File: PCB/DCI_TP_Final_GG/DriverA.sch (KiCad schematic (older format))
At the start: 18 parts

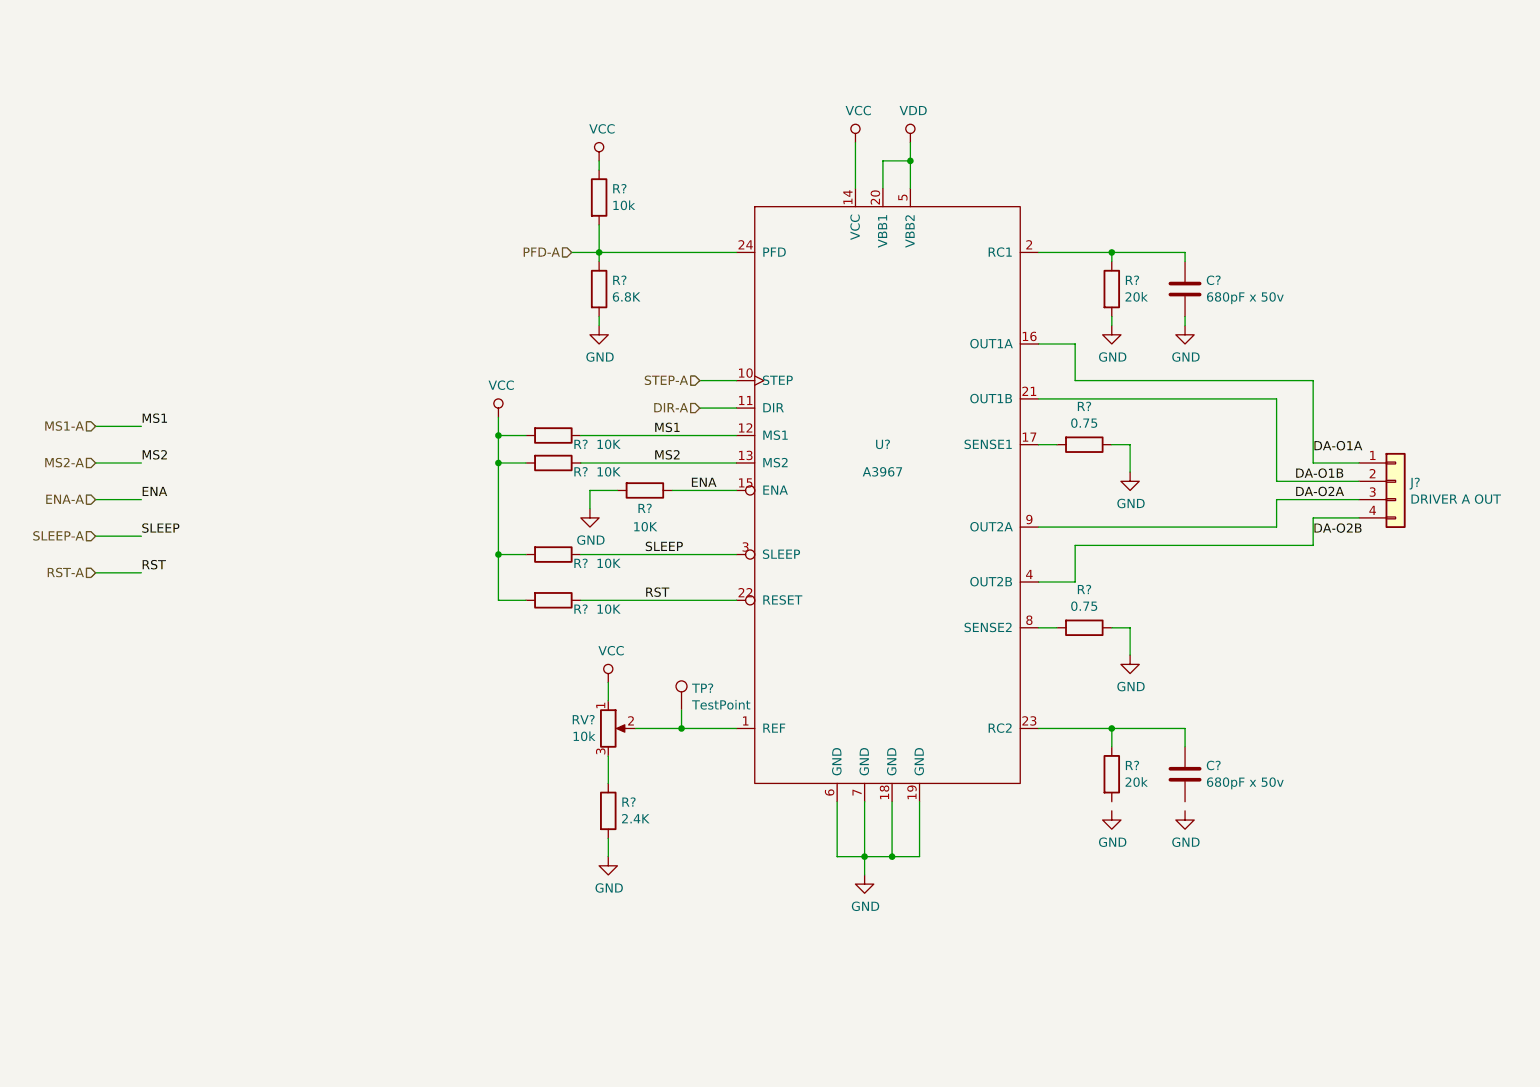
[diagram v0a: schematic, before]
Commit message: Hoja de fuente y conectores completa.
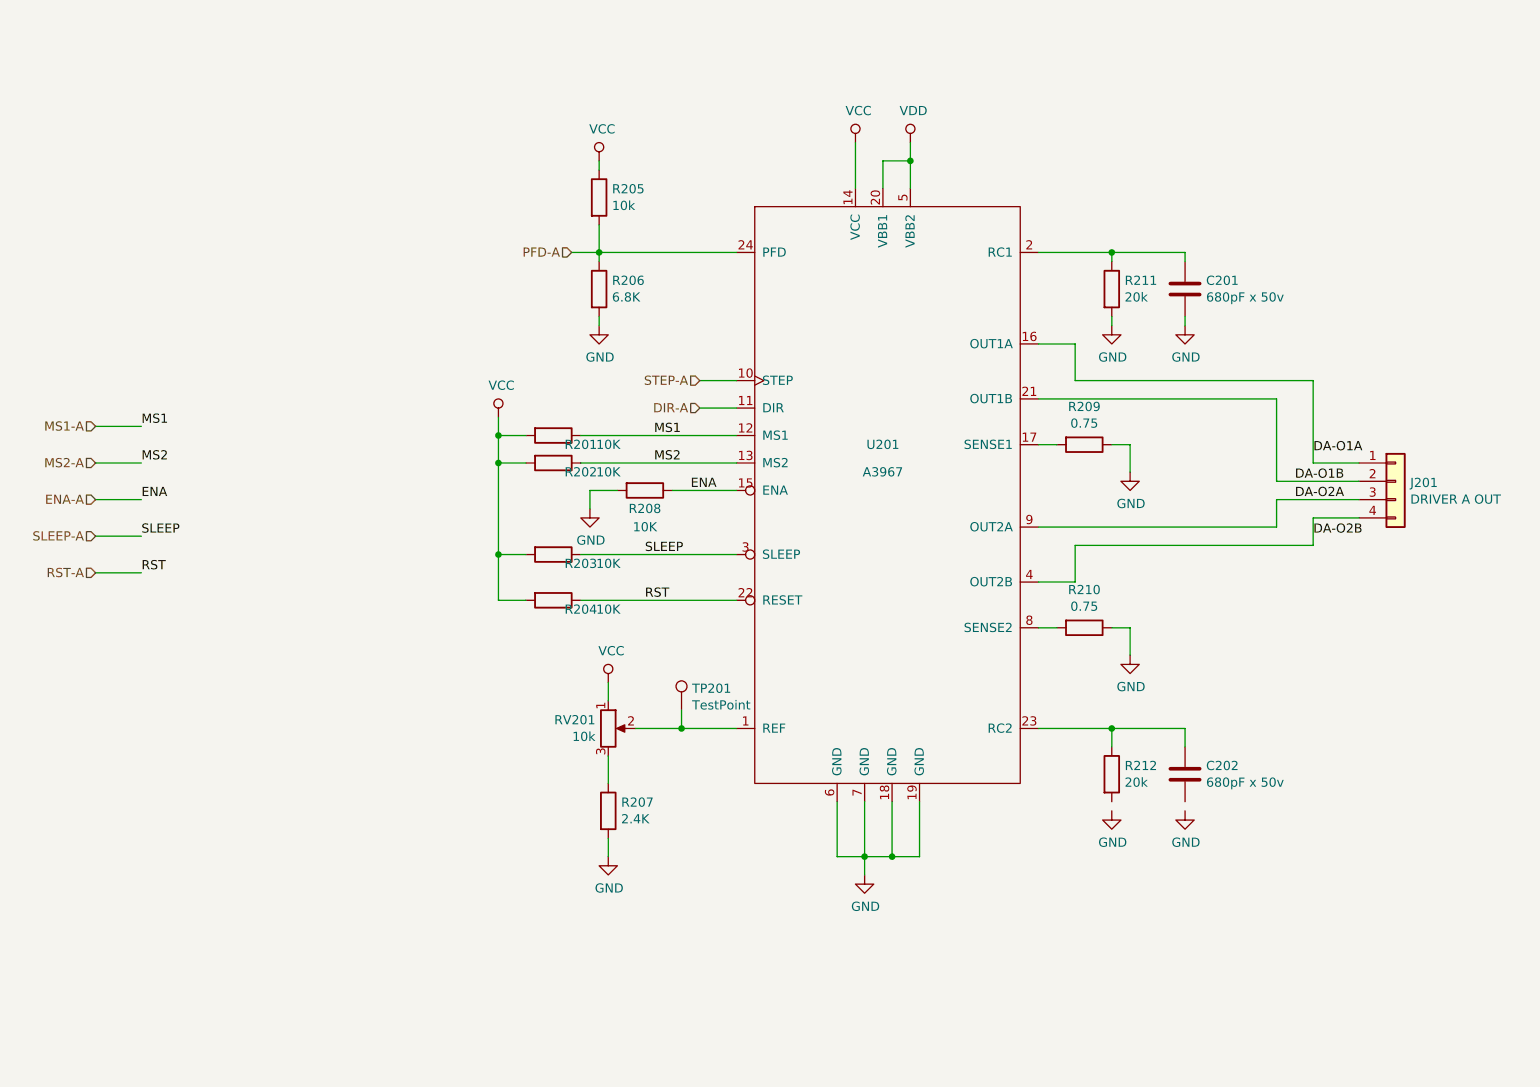
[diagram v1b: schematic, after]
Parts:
- TP201: renamed from TP?; footprint (none) -> TestPoint:TestPoint_Pad_D2.0mm
- gave numbers to parts that had none: 17
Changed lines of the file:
@@
 encoding utf-8
 Sheet 2 4
-Title ""
-Date ""
+Title "Replica Dual EasyDriver v4.5"
+Date "2019-10-02"
 Rev ""
-Comp ""
+Comp "Gonzalo Gontad - CESE-FIUBA"
 Comment1 ""
 Comment2 ""
@@
 $EndDescr
 $Comp
-L DCI_GG_CESE_FIUBA:A3967 U?
+L DCI_GG_CESE_FIUBA:A3967 U201
 U 1 1 5D973B9E
 P 3250 1150
-F 0 "U?" H 5800 -1100 50  0000 C CNN
+F 0 "U201" H 5800 -1100 50  0000 C CNN
 F 1 "A3967" H 5800 -1250 50  0000 C CNN
 F 2 "Package_SO:SOIC-24W_7.5x15.4mm_P1.27mm" V 6100 -1300 50  0001 C CNN
@@
 Connection ~ 5850 5650
 $Comp
-L power:GND #PWR?
+L power:GND #PWR0208
 U 1 1 5D96B0D6
 P 5700 5750
-F 0 "#PWR?" H 5700 5500 50  0001 C CNN
+F 0 "#PWR0208" H 5700 5500 50  0001 C CNN
 F 1 "GND" H 5705 5577 50  0000 C CNN
 F 2 "" H 5700 5750 50  0001 C CNN
@@
 	5700 5750 5700 5650
 $Comp
-L power:VCC #PWR?
+L power:VCC #PWR0207
 U 1 1 5D96D6E9
 P 5650 1750
-F 0 "#PWR?" H 5650 1600 50  0001 C CNN
+F 0 "#PWR0207" H 5650 1600 50  0001 C CNN
 F 1 "VCC" H 5667 1923 50  0000 C CNN
 F 2 "" H 5650 1750 50  0001 C CNN
@@
 $EndComp
 $Comp
-L power:VDD #PWR?
+L power:VDD #PWR0209
 U 1 1 5D96DCE4
 P 5950 1750
-F 0 "#PWR?" H 5950 1600 50  0001 C CNN
+F 0 "#PWR0209" H 5950 1600 50  0001 C CNN
 F 1 "VDD" H 5967 1923 50  0000 C CNN
 F 2 "" H 5950 1750 50  0001 C CNN
@@
 	5950 1850 5950 1750
 $Comp
-L Connector_Generic:Conn_01x04 J?
+L Connector_Generic:Conn_01x04 J201
 U 1 1 5D96F0CD
 P 8600 3600
-F 0 "J?" H 8680 3592 50  0000 L CNN
+F 0 "J201" H 8680 3592 50  0000 L CNN
 F 1 "DRIVER A OUT" H 8680 3501 50  0000 L CNN
 F 2 "TerminalBlock:TerminalBlock_Altech_AK300-4_P5.00mm" H 8600 3600 50  0001 C CNN
@@
 	6650 3850 7950 3850
 $Comp
-L Device:R R?
+L Device:R R209
 U 1 1 5D9772A0
 P 6900 3400
-F 0 "R?" V 6693 3400 50  0000 C CNN
+F 0 "R209" V 6693 3400 50  0000 C CNN
 F 1 "0.75" V 6784 3400 50  0000 C CNN
 F 2 "Resistor_SMD:R_0805_2012Metric" V 6830 3400 50  0001 C CNN
@@
 $EndComp
 $Comp
-L Device:R R?
+L Device:R R210
 U 1 1 5D977AE8
 P 6900 4400
-F 0 "R?" V 6693 4400 50  0000 C CNN
+F 0 "R210" V 6693 4400 50  0000 C CNN
 F 1 "0.75" V 6784 4400 50  0000 C CNN
 F 2 "Resistor_SMD:R_0805_2012Metric" V 6830 4400 50  0001 C CNN
@@
 $EndComp
 $Comp
-L power:GND #PWR?
+L power:GND #PWR0213
 U 1 1 5D978265
 P 7150 4550
-F 0 "#PWR?" H 7150 4300 50  0001 C CNN
+F 0 "#PWR0213" H 7150 4300 50  0001 C CNN
 F 1 "GND" H 7155 4377 50  0000 C CNN
 F 2 "" H 7150 4550 50  0001 C CNN
@@
 $EndComp
 $Comp
-L power:GND #PWR?
+L power:GND #PWR0212
 U 1 1 5D978D58
 P 7150 3550
-F 0 "#PWR?" H 7150 3300 50  0001 C CNN
+F 0 "#PWR0212" H 7150 3300 50  0001 C CNN
 F 1 "GND" H 7155 3377 50  0000 C CNN
 F 2 "" H 7150 3550 50  0001 C CNN
@@
 	7150 4400 7150 4550
 $Comp
-L Device:R R?
+L Device:R R212
 U 1 1 5D97A873
 P 7050 5200
-F 0 "R?" H 7120 5246 50  0000 L CNN
+F 0 "R212" H 7120 5246 50  0000 L CNN
 F 1 "20k" H 7120 5155 50  0000 L CNN
 F 2 "Resistor_SMD:R_0805_2012Metric" V 6980 5200 50  0001 C CNN
@@
 $EndComp
 $Comp
-L Device:C C?
+L Device:C C202
 U 1 1 5D97AE7B
 P 7450 5200
-F 0 "C?" H 7565 5246 50  0000 L CNN
+F 0 "C202" H 7565 5246 50  0000 L CNN
 F 1 "680pF x 50v" H 7565 5155 50  0000 L CNN
 F 2 "Capacitor_SMD:C_0805_2012Metric" H 7488 5050 50  0001 C CNN
@@
 $EndComp
 $Comp
-L Device:R R?
+L Device:R R211
 U 1 1 5D97D707
 P 7050 2550
-F 0 "R?" H 7120 2596 50  0000 L CNN
+F 0 "R211" H 7120 2596 50  0000 L CNN
 F 1 "20k" H 7120 2505 50  0000 L CNN
 F 2 "Resistor_SMD:R_0805_2012Metric" V 6980 2550 50  0001 C CNN
@@
 $EndComp
 $Comp
-L Device:C C?
+L Device:C C201
 U 1 1 5D97D712
 P 7450 2550
-F 0 "C?" H 7565 2596 50  0000 L CNN
+F 0 "C201" H 7565 2596 50  0000 L CNN
 F 1 "680pF x 50v" H 7565 2505 50  0000 L CNN
 F 2 "Capacitor_SMD:C_0805_2012Metric" H 7488 2400 50  0001 C CNN
@@
 $EndComp
 $Comp
-L power:GND #PWR?
+L power:GND #PWR0210
 U 1 1 5D9821C6
 P 7050 2750
-F 0 "#PWR?" H 7050 2500 50  0001 C CNN
+F 0 "#PWR0210" H 7050 2500 50  0001 C CNN
 F 1 "GND" H 7055 2577 50  0000 C CNN
 F 2 "" H 7050 2750 50  0001 C CNN
@@
 $EndComp
 $Comp
-L power:GND #PWR?
+L power:GND #PWR0214
 U 1 1 5D982982
 P 7450 2750
-F 0 "#PWR?" H 7450 2500 50  0001 C CNN
+F 0 "#PWR0214" H 7450 2500 50  0001 C CNN
 F 1 "GND" H 7455 2577 50  0000 C CNN
 F 2 "" H 7450 2750 50  0001 C CNN
@@
 $EndComp
 $Comp
-L power:GND #PWR?
+L power:GND #PWR0211
 U 1 1 5D982F91
 P 7050 5400
-F 0 "#PWR?" H 7050 5150 50  0001 C CNN
+F 0 "#PWR0211" H 7050 5150 50  0001 C CNN
 F 1 "GND" H 7055 5227 50  0000 C CNN
 F 2 "" H 7050 5400 50  0001 C CNN
@@
 $EndComp
 $Comp
-L power:GND #PWR?
+L power:GND #PWR0215
 U 1 1 5D983199
 P 7450 5400
-F 0 "#PWR?" H 7450 5150 50  0001 C CNN
+F 0 "#PWR0215" H 7450 5150 50  0001 C CNN
 F 1 "GND" H 7455 5227 50  0000 C CNN
 F 2 "" H 7450 5400 50  0001 C CNN
@@
 	7050 4950 6650 4950
 $Comp
-L Device:R R?
+L Device:R R206
 U 1 1 5D9954A4
 P 4250 2550
-F 0 "R?" H 4320 2596 50  0000 L CNN
+F 0 "R206" H 4320 2596 50  0000 L CNN
 F 1 "6.8K" H 4320 2505 50  0000 L CNN
 F 2 "Resistor_SMD:R_0805_2012Metric" V 4180 2550 50  0001 C CNN
@@
 $EndComp
 $Comp
-L Device:R R?
+L Device:R R205
 U 1 1 5D997CC8
 P 4250 2050
-F 0 "R?" H 4320 2096 50  0000 L CNN
+F 0 "R205" H 4320 2096 50  0000 L CNN
 F 1 "10k" H 4320 2005 50  0000 L CNN
 F 2 "Resistor_SMD:R_0805_2012Metric" V 4180 2050 50  0001 C CNN
@@
 $EndComp
 $Comp
-L power:GND #PWR?
+L power:GND #PWR0204
 U 1 1 5D9982F2
 P 4250 2750
-F 0 "#PWR?" H 4250 2500 50  0001 C CNN
+F 0 "#PWR0204" H 4250 2500 50  0001 C CNN
 F 1 "GND" H 4255 2577 50  0000 C CNN
 F 2 "" H 4250 2750 50  0001 C CNN
@@
 $EndComp
 $Comp
-L power:VCC #PWR?
+L power:VCC #PWR0203
 U 1 1 5D998ACC
 P 4250 1850
-F 0 "#PWR?" H 4250 1700 50  0001 C CNN
+F 0 "#PWR0203" H 4250 1700 50  0001 C CNN
 F 1 "VCC" H 4267 2023 50  0000 C CNN
 F 2 "" H 4250 1850 50  0001 C CNN
@@
 	4250 1850 4250 1900
 $Comp
-L Device:R_POT RV?
+L Device:R_POT RV201
 U 1 1 5D9A1651
 P 4300 4950
-F 0 "RV?" H 4230 4996 50  0000 R CNN
+F 0 "RV201" H 4230 4996 50  0000 R CNN
 F 1 "10k" H 4230 4905 50  0000 R CNN
 F 2 "Potentiometer_SMD:Potentiometer_Vishay_TS53YJ_Vertical" H 4300 4950 50  0001 C CNN
@@
 $EndComp
 $Comp
-L Device:R R?
+L Device:R R207
 U 1 1 5D9A2466
 P 4300 5400
-F 0 "R?" H 4370 5446 50  0000 L CNN
+F 0 "R207" H 4370 5446 50  0000 L CNN
 F 1 "2.4K" H 4370 5355 50  0000 L CNN
 F 2 "Resistor_SMD:R_0805_2012Metric" V 4230 5400 50  0001 C CNN
@@
 $EndComp
 $Comp
-L power:GND #PWR?
+L power:GND #PWR0206
 U 1 1 5D9A2951
 P 4300 5650
-F 0 "#PWR?" H 4300 5400 50  0001 C CNN
+F 0 "#PWR0206" H 4300 5400 50  0001 C CNN
 F 1 "GND" H 4305 5477 50  0000 C CNN
 F 2 "" H 4300 5650 50  0001 C CNN
@@
 $EndComp
 $Comp
-L power:VCC #PWR?
+L power:VCC #PWR0205
 U 1 1 5D9A2DAA
 P 4300 4700
-F 0 "#PWR?" H 4300 4550 50  0001 C CNN
+F 0 "#PWR0205" H 4300 4550 50  0001 C CNN
 F 1 "VCC" H 4317 4873 50  0000 C CNN
 F 2 "" H 4300 4700 50  0001 C CNN
@@
 $EndComp
 $Comp
-L Connector:TestPoint TP?
+L Connector:TestPoint TP201
 U 1 1 5D9A33E4
 P 4700 4850
-F 0 "TP?" H 4758 4968 50  0000 L CNN
+F 0 "TP201" H 4758 4968 50  0000 L CNN
 F 1 "TestPoint" H 4758 4877 50  0000 L CNN
-F 2 "" H 4900 4850 50  0001 C CNN
+F 2 "TestPoint:TestPoint_Pad_D2.0mm" H 4900 4850 50  0001 C CNN
 F 3 "~" H 4900 4850 50  0001 C CNN
 	1    4700 4850
@@
 	4700 4950 4450 4950
 $Comp
-L Device:R R?
+L Device:R R208
 U 1 1 5D9AD238
 P 4500 3650
-F 0 "R?" V 4600 3650 50  0000 C CNN
+F 0 "R208" V 4600 3650 50  0000 C CNN
 F 1 "10K" V 4700 3650 50  0000 C CNN
 F 2 "Resistor_SMD:R_0805_2012Metric" V 4430 3650 50  0001 C CNN
@@
 $EndComp
 $Comp
-L power:GND #PWR?
+L power:GND #PWR0202
 U 1 1 5D9ADB97
 P 4200 3750
-F 0 "#PWR?" H 4200 3500 50  0001 C CNN
+F 0 "#PWR0202" H 4200 3500 50  0001 C CNN
 F 1 "GND" H 4205 3577 50  0000 C CNN
 F 2 "" H 4200 3750 50  0001 C CNN
@@
 	4200 3650 4200 3750
 $Comp
-L Device:R R?
+L Device:R R202
 U 1 1 5D9B1238
 P 4000 3500
-F 0 "R?" V 4050 3650 50  0000 C CNN
+F 0 "R202" V 4050 3650 50  0000 C CNN
 F 1 "10K" V 4050 3800 50  0000 C CNN
 F 2 "Resistor_SMD:R_0805_2012Metric" V 3930 3500 50  0001 C CNN
@@
 $EndComp
 $Comp
-L Device:R R?
+L Device:R R201
 U 1 1 5D9B192B
 P 4000 3350
-F 0 "R?" V 4050 3500 50  0000 C CNN
+F 0 "R201" V 4050 3500 50  0000 C CNN
 F 1 "10K" V 4050 3650 50  0000 C CNN
 F 2 "Resistor_SMD:R_0805_2012Metric" V 3930 3350 50  0001 C CNN
@@
 	4150 3500 5000 3500
 $Comp
-L Device:R R?
+L Device:R R203
 U 1 1 5D9B8041
 P 4000 4000
-F 0 "R?" V 4050 4150 50  0000 C CNN
+F 0 "R203" V 4050 4150 50  0000 C CNN
 F 1 "10K" V 4050 4300 50  0000 C CNN
 F 2 "Resistor_SMD:R_0805_2012Metric" V 3930 4000 50  0001 C CNN
@@
 $EndComp
 $Comp
-L Device:R R?
+L Device:R R204
 U 1 1 5D9B8586
 P 4000 4250
-F 0 "R?" V 4050 4400 50  0000 C CNN
+F 0 "R204" V 4050 4400 50  0000 C CNN
 F 1 "10K" V 4050 4550 50  0000 C CNN
 F 2 "Resistor_SMD:R_0805_2012Metric" V 3930 4250 50  0001 C CNN
@@
 	3700 3500 3700 4000
 $Comp
-L power:VCC #PWR?
+L power:VCC #PWR0201
 U 1 1 5D9C167C
 P 3700 3250
-F 0 "#PWR?" H 3700 3100 50  0001 C CNN
+F 0 "#PWR0201" H 3700 3100 50  0001 C CNN
 F 1 "VCC" H 3717 3423 50  0000 C CNN
 F 2 "" H 3700 3250 50  0001 C CNN

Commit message: Se completo el esquematico y documentación. El esquematico esta listo para una primera revisión.
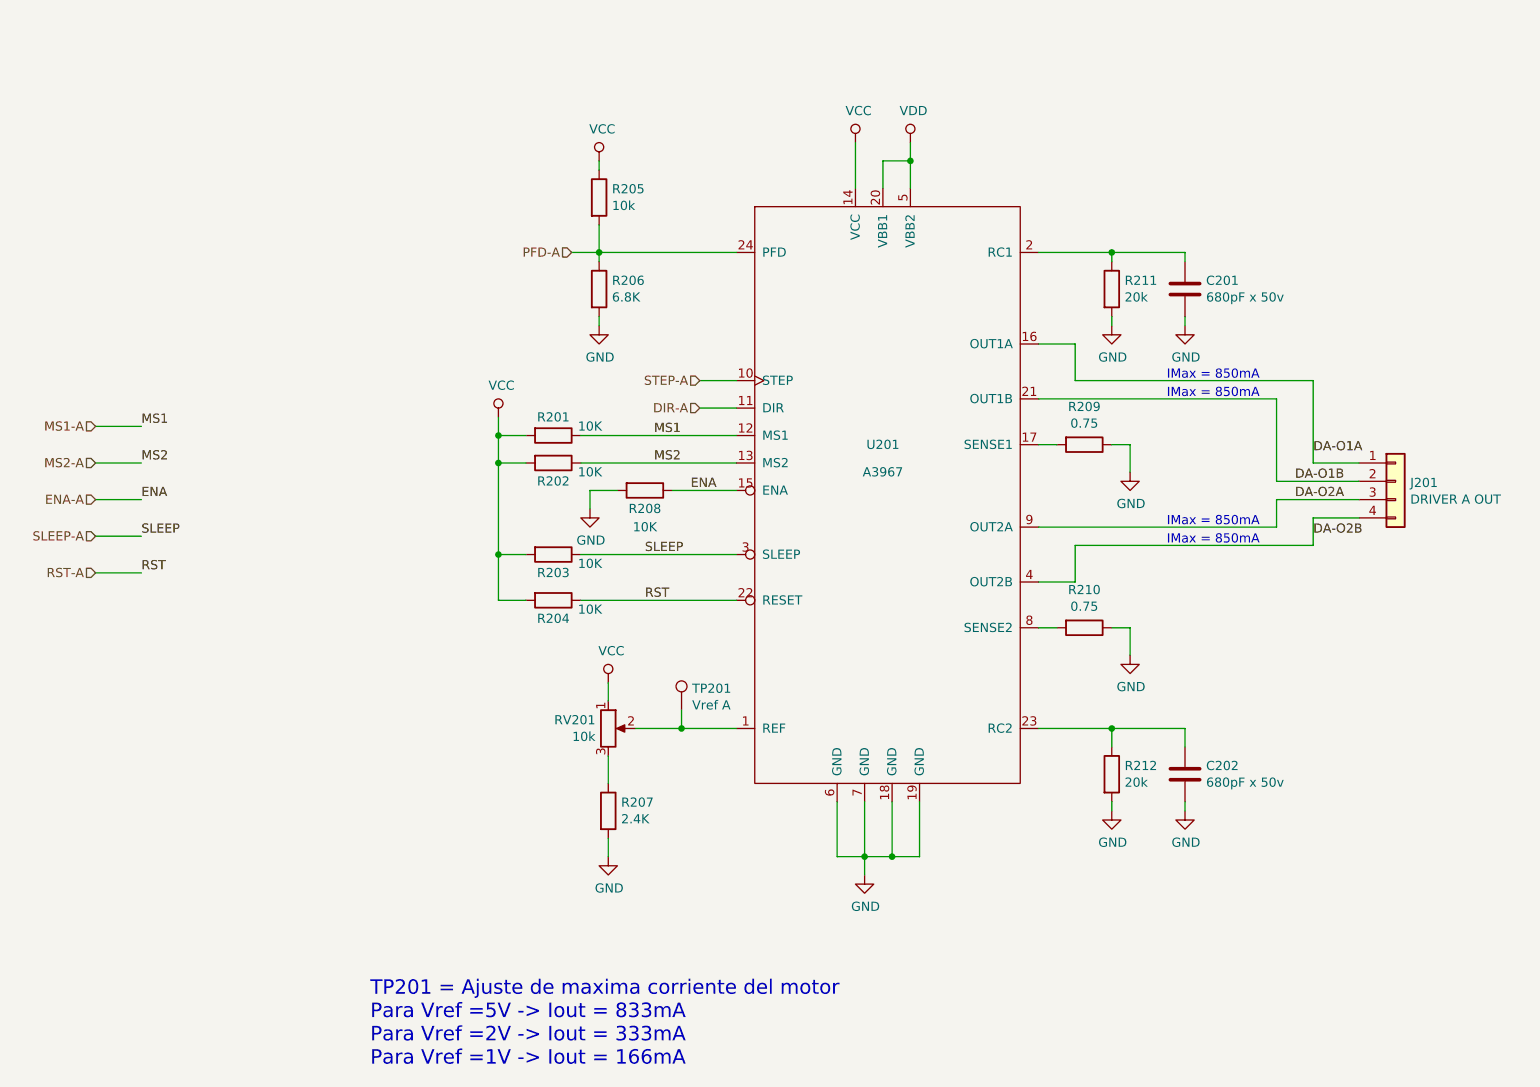
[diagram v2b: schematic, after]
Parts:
- TP201: value TestPoint -> Vref A
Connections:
- net GND: now also C202.2, R212.2
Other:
- note added: "IMax = 850mA"
- note added: "TP201 = Ajuste de maxima corriente del motor\nPara Vref =5V -> Iout = 833mA\nPara Vref =2V -> Iout = 333mA\nPara Vref =1V -> Iout = 166mA"
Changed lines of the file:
@@
 P 4700 4850
 F 0 "TP201" H 4758 4968 50  0000 L CNN
-F 1 "TestPoint" H 4758 4877 50  0000 L CNN
+F 1 "Vref A" H 4758 4877 50  0000 L CNN
 F 2 "TestPoint:TestPoint_Pad_D2.0mm" H 4900 4850 50  0001 C CNN
 F 3 "~" H 4900 4850 50  0001 C CNN
@@
 U 1 1 5D9B1238
 P 4000 3500
-F 0 "R202" V 4050 3650 50  0000 C CNN
-F 1 "10K" V 4050 3800 50  0000 C CNN
+F 0 "R202" V 4100 3500 50  0000 C CNN
+F 1 "10K" V 4050 3700 50  0000 C CNN
 F 2 "Resistor_SMD:R_0805_2012Metric" V 3930 3500 50  0001 C CNN
 F 3 "" H 4000 3500 50  0001 C CNN
@@
 U 1 1 5D9B192B
 P 4000 3350
-F 0 "R201" V 4050 3500 50  0000 C CNN
-F 1 "10K" V 4050 3650 50  0000 C CNN
+F 0 "R201" V 3900 3350 50  0000 C CNN
+F 1 "10K" V 3950 3550 50  0000 C CNN
 F 2 "Resistor_SMD:R_0805_2012Metric" V 3930 3350 50  0001 C CNN
 F 3 "" H 4000 3350 50  0001 C CNN
@@
 U 1 1 5D9B8041
 P 4000 4000
-F 0 "R203" V 4050 4150 50  0000 C CNN
-F 1 "10K" V 4050 4300 50  0000 C CNN
+F 0 "R203" V 4100 4000 50  0000 C CNN
+F 1 "10K" V 4050 4200 50  0000 C CNN
 F 2 "Resistor_SMD:R_0805_2012Metric" V 3930 4000 50  0001 C CNN
 F 3 "" H 4000 4000 50  0001 C CNN
@@
 U 1 1 5D9B8586
 P 4000 4250
-F 0 "R204" V 4050 4400 50  0000 C CNN
-F 1 "10K" V 4050 4550 50  0000 C CNN
+F 0 "R204" V 4100 4250 50  0000 C CNN
+F 1 "10K" V 4050 4450 50  0000 C CNN
 F 2 "Resistor_SMD:R_0805_2012Metric" V 3930 4250 50  0001 C CNN
 F 3 "" H 4000 4250 50  0001 C CNN
@@
 Text Label 8150 3900 0    50   ~ 0
 DA-O2B
+Wire Wire Line
+	7450 5350 7450 5400
+Wire Wire Line
+	7050 5350 7050 5400
+Text Notes 7350 3050 0    50   ~ 0
+IMax = 850mA
+Text Notes 7350 3150 0    50   ~ 0
+IMax = 850mA
+Text Notes 7350 3850 0    50   ~ 0
+IMax = 850mA
+Text Notes 7350 3950 0    50   ~ 0
+IMax = 850mA
+Text Notes 3000 6800 0    79   ~ 0
+TP201 = Ajuste de maxima corriente del motor\nPara Vref =5V -> Iout = 833mA\nPara Vref =2V -> Iout = 333mA\nPara Vref =1V -> Iout = 166mA
 $EndSCHEMATC

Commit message: Inicio etapa de desarrollo de PCB, agrego biblioteca de borneras
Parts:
- J201: footprint TerminalBlock:TerminalBlock_Altech_AK300-4_P5.00mm -> TerminalBlock_Phoenix:TerminalBlock_Phoenix_MKDS-1,5-4_1x04_P5.00mm_Horizontal
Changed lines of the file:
@@
 F 0 "J201" H 8680 3592 50  0000 L CNN
 F 1 "DRIVER A OUT" H 8680 3501 50  0000 L CNN
-F 2 "TerminalBlock:TerminalBlock_Altech_AK300-4_P5.00mm" H 8600 3600 50  0001 C CNN
+F 2 "TerminalBlock_Phoenix:TerminalBlock_Phoenix_MKDS-1,5-4_1x04_P5.00mm_Horizontal" H 8600 3600 50  0001 C CNN
 F 3 "~" H 8600 3600 50  0001 C CNN
 	1    8600 3600

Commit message: Agrego 3D de borneras
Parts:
- RV201: #Fab (none) -> TS53YJ103MR10; Digikey (none) -> TS53YJ-10KTR-ND
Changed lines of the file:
@@
 F 2 "Potentiometer_SMD:Potentiometer_Vishay_TS53YJ_Vertical" H 4300 4950 50  0001 C CNN
 F 3 "" H 4300 4950 50  0001 C CNN
+F 4 "TS53YJ-10KTR-ND" H 4300 4950 50  0001 C CNN "Digikey"
+F 5 "TS53YJ103MR10" H 4300 4950 50  0001 C CNN "#Fab"
 	1    4300 4950
 	1    0    0    -1
